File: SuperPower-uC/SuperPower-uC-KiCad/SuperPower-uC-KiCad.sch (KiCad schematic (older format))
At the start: 0 parts

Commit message: Actually saved the changes as well
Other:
- note added: "3v3_LDO"
- note added: "3v3_LDO_MCU"
- note added: "5V Buck/Boost"
- note added: "Battery Holder"
- note added: "Battery Protection"
- note added: "Charger"
- note added: "Cut-Off Circuit"
- note added: "Fuel Gauge"
- note added: "MCU"
- note added: "Manual Wake"
- note added: "RTC"
- note added: "Screw Terminal"
- note added: "Solder Pads"
- note added: "USB-C"
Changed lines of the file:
@@
 F5 "VOUT" O R 4300 2550 50
 F6 "VBAT" B L 3050 2550 50
+F7 "SCL" I R 4300 3050 50
+F8 "SDA" I R 4300 3150 50
 $EndSheet
 $Sheet
-S 4900 4000 1250 1150
+S 4950 4000 1250 1150
 U 5F63A00B
 F0 "RTC and Cut-Off Module" 50
 F1 "rtc_cut_off.sch" 50
+F2 "SCL" I R 6200 4100 50
+F3 "SDA" B R 6200 4200 50
+F4 "VIN" I L 4950 4650 50
+F5 "VOUT" O L 4950 4450 50
 $EndSheet
 $Sheet
@@
 F0 "MCU Module" 50
 F1 "mcu.sch" 50
+F2 "3v3_MCU" I L 6850 2850 50
+F3 "SDA" B L 6850 3150 50
+F4 "SCL" I L 6850 3050 50
+F5 "D+" I R 8100 3150 50
+F6 "D-" I R 8100 3050 50
 $EndSheet
 $Sheet
@@
 F3 "VSOLAR" O L 3050 4350 50
 F4 "VOUT" O L 3050 4500 50
+F5 "D+" I R 4300 4900 50
+F6 "D-" I R 4300 5000 50
 $EndSheet
 Wire Wire Line
@@
 	2550 2550 3050 2550
 Wire Wire Line
-	4300 2550 4900 2550
-Text HLabel 6850 2850 2    50   Input ~ 0
-3v3_MCU
+	6850 2850 6150 2850
 Wire Wire Line
-	6850 2850 6150 2850
+	6850 3150 6650 3150
+Wire Wire Line
+	6650 3150 6650 3550
+Wire Wire Line
+	6650 4200 6200 4200
+Wire Wire Line
+	6850 3050 6600 3050
+Wire Wire Line
+	6600 3050 6600 3500
+Wire Wire Line
+	6600 4100 6200 4100
+Wire Wire Line
+	4300 2550 4550 2550
+Wire Wire Line
+	4550 2550 4550 4650
+Wire Wire Line
+	4550 4650 4950 4650
+Wire Wire Line
+	4950 4450 4700 4450
+Wire Wire Line
+	4700 4450 4700 2550
+Wire Wire Line
+	4700 2550 4900 2550
+Text Notes 1400 2300 0    50   ~ 0
+Battery Holder
+Text Notes 1400 2450 0    50   ~ 0
+Battery Protection
+Text Notes 3450 2300 0    50   ~ 0
+Charger
+Text Notes 3450 2400 0    50   ~ 0
+Fuel Gauge
+Text Notes 5150 2300 0    50   ~ 0
+3v3_LDO
+Text Notes 5150 2400 0    50   ~ 0
+3v3_LDO_MCU
+Text Notes 5150 2500 0    50   ~ 0
+5V Buck/Boost
+Text Notes 7400 2450 0    50   ~ 0
+MCU
+Text Notes 5350 4350 0    50   ~ 0
+RTC
+Text Notes 5350 4450 0    50   ~ 0
+Cut-Off Circuit
+Text Notes 3600 4350 0    50   ~ 0
+USB-C
+Text Notes 3600 4450 0    50   ~ 0
+Screw Terminal
+Text Notes 3600 4550 0    50   ~ 0
+Solder Pads
+Wire Wire Line
+	4300 3050 4450 3050
+Wire Wire Line
+	4450 3050 4450 3500
+Wire Wire Line
+	4450 3500 6600 3500
+Connection ~ 6600 3500
+Wire Wire Line
+	6600 3500 6600 4100
+Wire Wire Line
+	4300 3150 4400 3150
+Wire Wire Line
+	4400 3150 4400 3550
+Wire Wire Line
+	4400 3550 6650 3550
+Connection ~ 6650 3550
+Wire Wire Line
+	6650 3550 6650 4200
+Text Notes 5350 4550 0    50   ~ 0
+Manual Wake
+Wire Wire Line
+	8100 3150 8350 3150
+Wire Wire Line
+	8350 5400 4750 5400
+Wire Wire Line
+	4750 5400 4750 4900
+Wire Wire Line
+	4750 4900 4300 4900
+Wire Wire Line
+	8350 3150 8350 5400
+Wire Wire Line
+	8100 3050 8400 3050
+Wire Wire Line
+	8400 3050 8400 5450
+Wire Wire Line
+	8400 5450 4700 5450
+Wire Wire Line
+	4700 5450 4700 5000
+Wire Wire Line
+	4700 5000 4300 5000
 $EndSCHEMATC

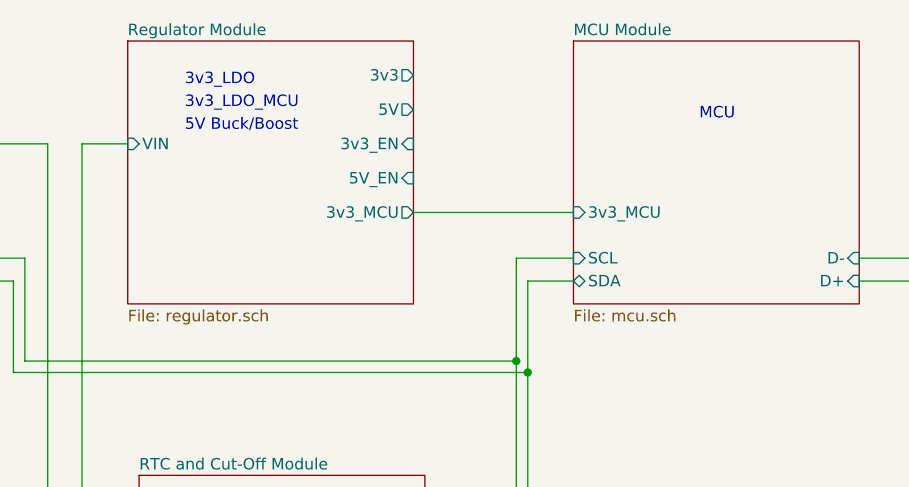
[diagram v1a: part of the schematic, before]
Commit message: Add some text and more architecture tracks
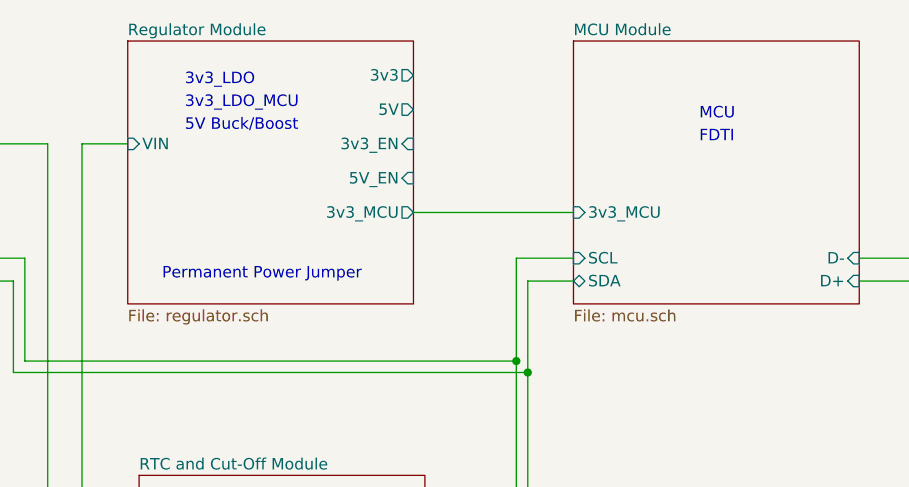
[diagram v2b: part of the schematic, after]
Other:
- note added: "FDTI"
- note added: "Permanent Power Jumper"
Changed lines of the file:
@@
 Wire Wire Line
 	4700 5000 4300 5000
+Text Notes 5050 3150 0    50   ~ 0
+Permanent Power Jumper
+Text Notes 7400 2550 0    50   ~ 0
+FDTI
 $EndSCHEMATC

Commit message: Add gitignore + smaller changes to the draft
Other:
- note added: "Bypass Jumper"
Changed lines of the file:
@@
 EESchema Schematic File Version 4
+LIBS:SuperPower-uC-KiCad-cache
 EELAYER 29 0
 EELAYER END
@@
 Text Notes 7400 2550 0    50   ~ 0
 FDTI
+Text Notes 5350 4650 0    50   ~ 0
+Bypass Jumper
 $EndSCHEMATC
